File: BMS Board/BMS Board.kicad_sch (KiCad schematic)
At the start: 196 parts, among them Q1 NMOS, U1 BQ76920PW, U2 TCA9548APWR, U3 BQ76920PW, U4 BQ76920PW, U5 BQ76920PW, U6 BQ76920PW, U7 BQ76920PW, U8 BQ76920PW, U9 BQ76930DBT

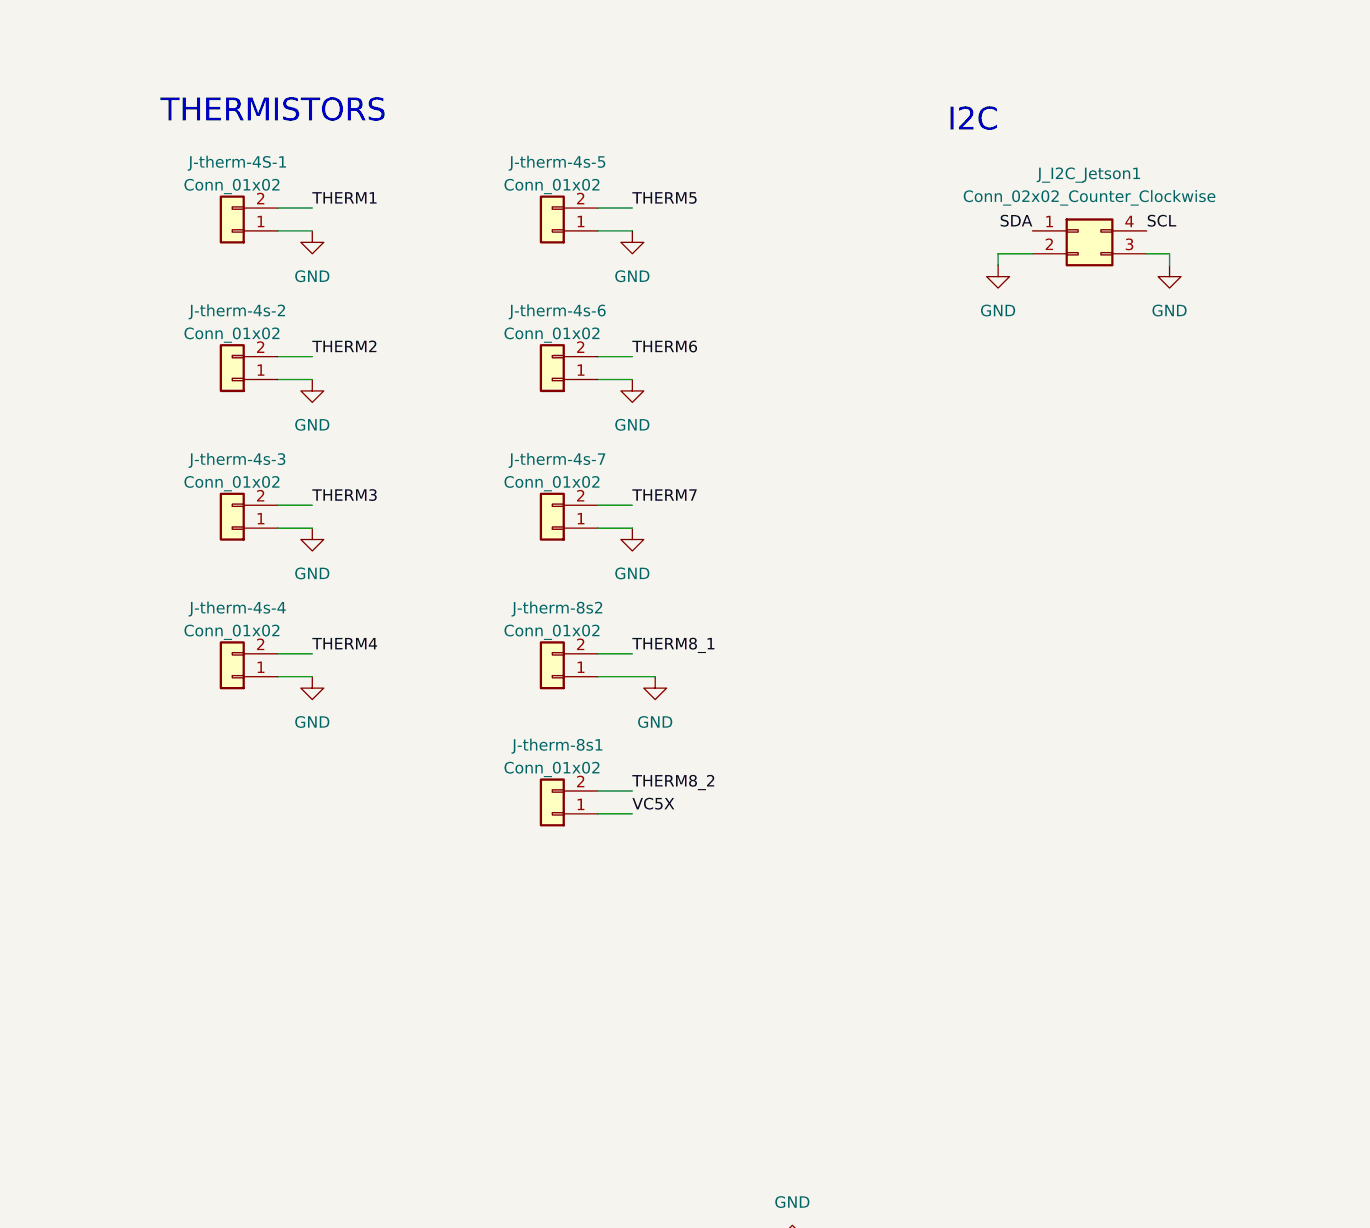
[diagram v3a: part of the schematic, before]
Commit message: BMS layout for three batteries done
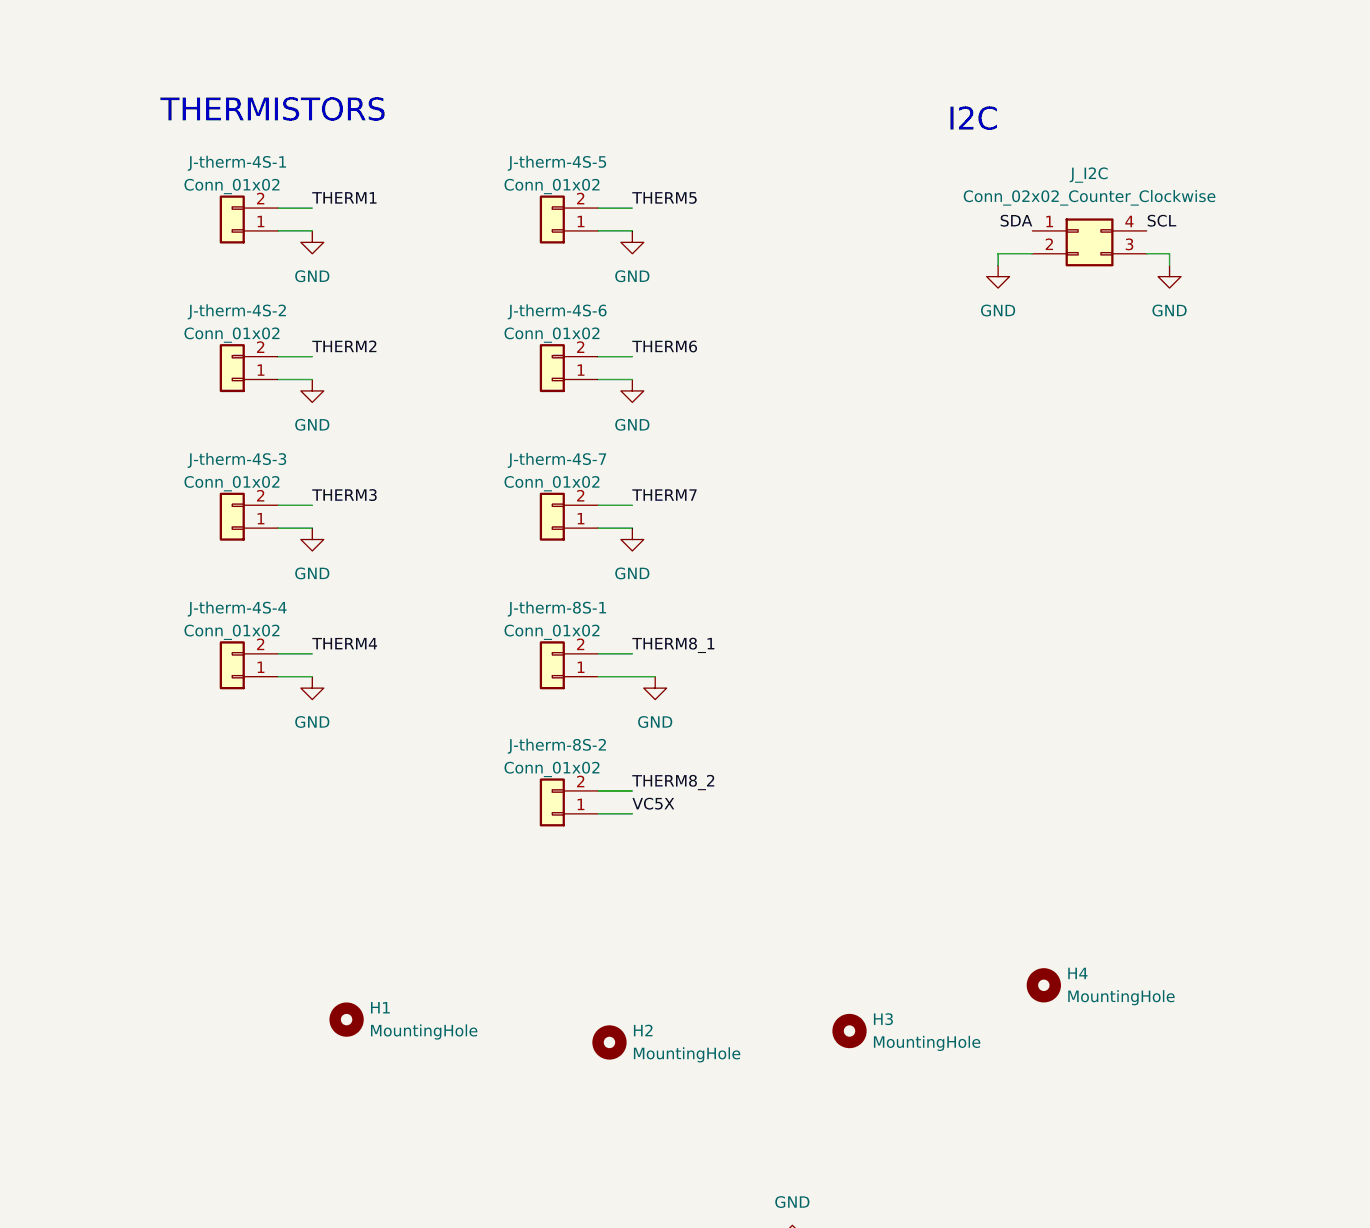
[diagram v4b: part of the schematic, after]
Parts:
- added H1, H2, H3, H4: MountingHole, MountingHole:MountingHole_3.2mm_M3_DIN965, symbol Mechanical:MountingHole
- renumbered J-therm-4s-2 to J-therm-4S-2, J-therm-4s-3 to J-therm-4S-3, J-therm-4s-4 to J-therm-4S-4, J-therm-4s-5 to J-therm-4S-5, J-therm-4s-6 to J-therm-4S-6, J-therm-4s-7 to J-therm-4S-7, J-therm-8s2 to J-therm-8S-1, J-therm-8s1 to J-therm-8S-2, J_I2C_Jetson1 to J_I2C

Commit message: BMS pretty much completed
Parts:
- added C79, C80: 1uF, Capacitor_SMD:C_0603_1608Metric, symbol Device:C
- added J1: Conn_01x02, Connector_AMASS:AMASS_XT30UPB-F_1x02_P5.0mm_Vertical, symbol Connector_Generic:Conn_01x02
- added U10: TLV70033_SOT23-5, Package_TO_SOT_SMD:SOT-23-5, symbol Regulator_Linear:TLV70033_SOT23-5
- D1, D2: footprint (none) -> Diode_SMD:D_SOD-123
- J_I2C1: renamed from J_I2C; footprint (none) -> Connector_Molex:Molex_Nano-Fit_105309-xx04_1x04_P2.50mm_Vertical
- Q1: footprint (none) -> Package_TO_SOT_SMD:SOT-23
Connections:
- net 3.3V: now also C80.1, U10.5 (OUT)
- net 8S-VC0: now also J-8S0.1 (Pin_1)
- net 8S-VC1: now also J-8S0.2 (Pin_2)
- net 8S-VC2: now also J-8S0.3 (Pin_3)
- net 8S-VC3: now also J-8S0.4 (Pin_4)
- net 8S-VC4: now also J-8S0.5 (Pin_5), J-8S1.1 (Pin_1)
- net 8S-VC6: now also J-8S1.2 (Pin_2)
- net 8S-VC7: now also J-8S1.3 (Pin_3)
- net 8S-VC8: now also J-8S1.4 (Pin_4)
- net 8S-VC9: now also J-8S1.5 (Pin_5)
- net GND: now also C79.2, C80.2, J1.1 (Pin_1), U10.2 (GND)
- net SC0: now also R75.2, U2.9 (SC2); no longer R71.2, U2.5 (SC0)
- net SC1: now also R77.2, U2.11 (SC3); no longer R73.2, U2.7 (SC1)
- net SC2: now also R81.1, U2.16 (SC5); no longer R75.2, U2.9 (SC2)
- net SC3: now also R73.2, U2.7 (SC1); no longer R77.2, U2.11 (SC3)
- net SC5: now also R83.1, U2.18 (SC6); no longer R81.1, U2.16 (SC5)
- net SC6: now also R71.2, U2.5 (SC0); no longer R83.1, U2.18 (SC6)
- net SD0: now also R76.2, U2.8 (SD2); no longer R72.2, U2.4 (SD0)
- net SD1: now also R78.2, U2.10 (SD3); no longer R74.2, U2.6 (SD1)
- net SD2: now also R82.1, U2.15 (SD5); no longer R76.2, U2.8 (SD2)
- net SD3: now also R74.2, U2.6 (SD1); no longer R78.2, U2.10 (SD3)
- net SD5: now also R85.1, U2.17 (SD6); no longer R82.1, U2.15 (SD5)
- net SD6: now also R72.2, U2.4 (SD0); no longer R85.1, U2.17 (SD6)
- new net 5V: C79.1, J1.2 (Pin_2), U10.1 (IN)
- no-connect marks 16 -> 17
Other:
- moved on the sheet: H1, H2, H3, H4

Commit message: added LED to monitor 5v power
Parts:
- added D3: LED, Diode_SMD:D_0603_1608Metric, symbol Device:LED
- added R88: 1k, Resistor_SMD:R_0805_2012Metric, symbol Device:R
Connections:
- net 5V: now also R88.2
- net GND: now also D3.1 (K)
- new net: D3.2 (A), R88.1
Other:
- moved on the sheet: C79, C80, H1, H2, H3, H4, J-4S-5, J-4S-6, J-4S-7, J-8S0, J-8S1, J-therm-4S-1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

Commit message: added mounting holes
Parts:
- added H5, H6: MountingHole, MountingHole:MountingHole_3.2mm_M3_DIN965, symbol Mechanical:MountingHole
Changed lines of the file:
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@@
 	)
 	(symbol
+		(lib_id "Mechanical:MountingHole")
+		(at 259.08 110.49 0)
+		(unit 1)
+		(exclude_from_sim no)
+		(in_bom no)
+		(on_board yes)
+		(dnp no)
+		(fields_autoplaced yes)
+		(property "Reference" "H6"
+			(at 261.62 109.2199 0)
+			(effects
+				(font
+					(size 1.27 1.27)
+				)
+				(justify left)
+			)
+		)
+		(property "Value" "MountingHole"
+			(at 261.62 111.7599 0)
+			(effects
+				(font
+					(size 1.27 1.27)
+				)
+				(justify left)
+			)
+		)
+		(property "Footprint" "MountingHole:MountingHole_3.2mm_M3_DIN965"
+			(at 259.08 110.49 0)
+			(effects
+				(font
+					(size 1.27 1.27)
+				)
+				(hide yes)
+			)
+		)
+		(property "Datasheet" "~"
+			(at 259.08 110.49 0)
+			(effects
+				(font
+					(size 1.27 1.27)
+				)
+				(hide yes)
+			)
+		)
+		(property "Description" "Mounting Hole without connection"
+			(at 259.08 110.49 0)
+			(effects
+				(font
+					(size 1.27 1.27)
+				)
+				(hide yes)
+			)
+		)
+		(instances
+			(project "BMS Board"
+				(path "/a57f7fab-6172-446f-9361-69af31cdb407"
+					(reference "H6")
+					(unit 1)
+				)
+			)
+		)
+	)
+	(symbol
 		(lib_id "power:GND")
 		(at 52.07 266.7 270)
@@
 					(unit 1)
 				)
+			)
+		)
+	)
+	(symbol
+		(lib_id "Mechanical:MountingHole")
+		(at 259.08 101.6 0)
+		(unit 1)
+		(exclude_from_sim no)
+		(in_bom no)
+		(on_board yes)
+		(dnp no)
+		(fields_autoplaced yes)
+		(property "Reference" "H5"
+			(at 261.62 100.3299 0)
+			(effects
+				(font
+					(size 1.27 1.27)
+				)
+				(justify left)
+			)
+		)
+		(property "Value" "MountingHole"
+			(at 261.62 102.8699 0)
+			(effects
+				(font
+					(size 1.27 1.27)
+				)
+				(justify left)
+			)
+		)
+		(property "Footprint" "MountingHole:MountingHole_3.2mm_M3_DIN965"
+			(at 259.08 101.6 0)
+			(effects
+				(font
+					(size 1.27 1.27)
+				)
+				(hide yes)
+			)
+		)
+		(property "Datasheet" "~"
+			(at 259.08 101.6 0)
+			(effects
+				(font
+					(size 1.27 1.27)
+				)
+				(hide yes)
+			)
+		)
+		(property "Description" "Mounting Hole without connection"
+			(at 259.08 101.6 0)
+			(effects
+				(font
+					(size 1.27 1.27)
+				)
+				(hide yes)
+			)
+		)
+		(instances
+			(project "BMS Board"
+				(path "/a57f7fab-6172-446f-9361-69af31cdb407"
+					(reference "H5")
+					(unit 1)
+				)

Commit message: minor updates to BMS; edge cuts, GND pour, via stitching, missed connections for PDB
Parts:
- added H7: MountingHole, MountingHole:MountingHole_3.2mm_M3_DIN965, symbol Mechanical:MountingHole
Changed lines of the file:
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@@
+	)
+	(symbol
+		(lib_id "Mechanical:MountingHole")
+		(at 259.08 121.92 0)
+		(unit 1)
+		(exclude_from_sim no)
+		(in_bom no)
+		(on_board yes)
+		(dnp no)
+		(fields_autoplaced yes)
+		(property "Reference" "H7"
+			(at 261.62 120.6499 0)
+			(effects
+				(font
+					(size 1.27 1.27)
+				)
+				(justify left)
+			)
+		)
+		(property "Value" "MountingHole"
+			(at 261.62 123.1899 0)
+			(effects
+				(font
+					(size 1.27 1.27)
+				)
+				(justify left)
+			)
+		)
+		(property "Footprint" "MountingHole:MountingHole_3.2mm_M3_DIN965"
+			(at 259.08 121.92 0)
+			(effects
+				(font
+					(size 1.27 1.27)
+				)
+				(hide yes)
+			)
+		)
+		(property "Datasheet" "~"
+			(at 259.08 121.92 0)
+			(effects
+				(font
+					(size 1.27 1.27)
+				)
+				(hide yes)
+			)
+		)
+		(property "Description" "Mounting Hole without connection"
+			(at 259.08 121.92 0)
+			(effects
+				(font
+					(size 1.27 1.27)
+				)
+				(hide yes)
+			)
+		)
+		(instances
+			(project "BMS Board"
+				(path "/a57f7fab-6172-446f-9361-69af31cdb407"
+					(reference "H7")
+					(unit 1)
+				)
+			)
+		)
 	)
 	(symbol
